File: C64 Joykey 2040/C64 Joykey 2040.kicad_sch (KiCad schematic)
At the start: 21 parts, among them J4 Expansion, M1 Mounting, M2 Mounting, M3 Mounting, M4 Mounting, U1 RP2040-Zero

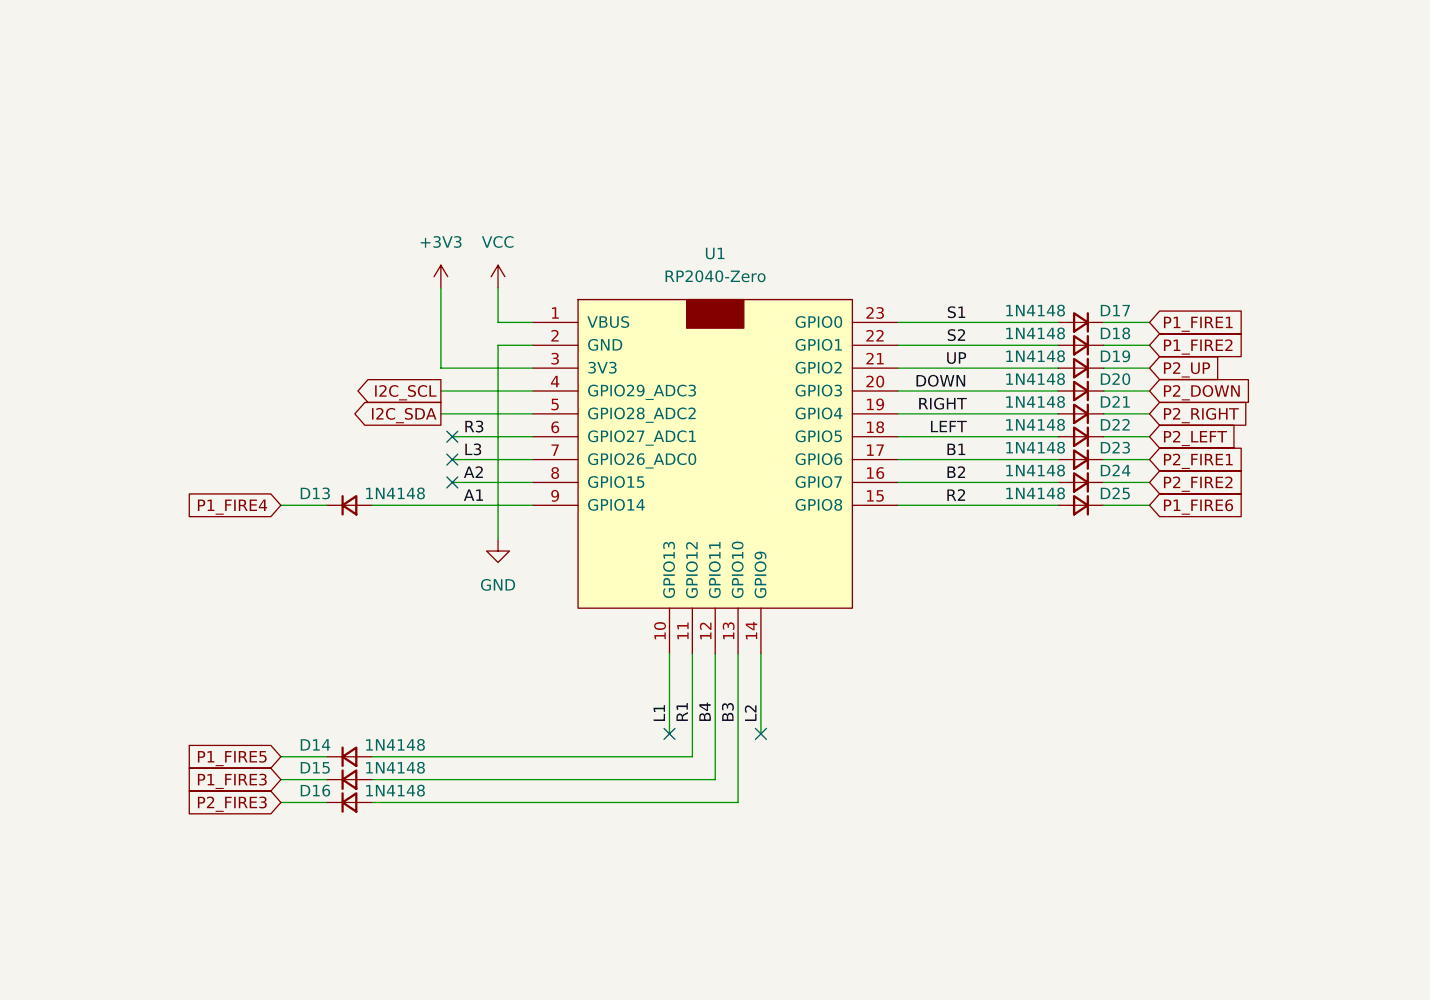
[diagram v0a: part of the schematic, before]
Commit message: Add diode for power from USB
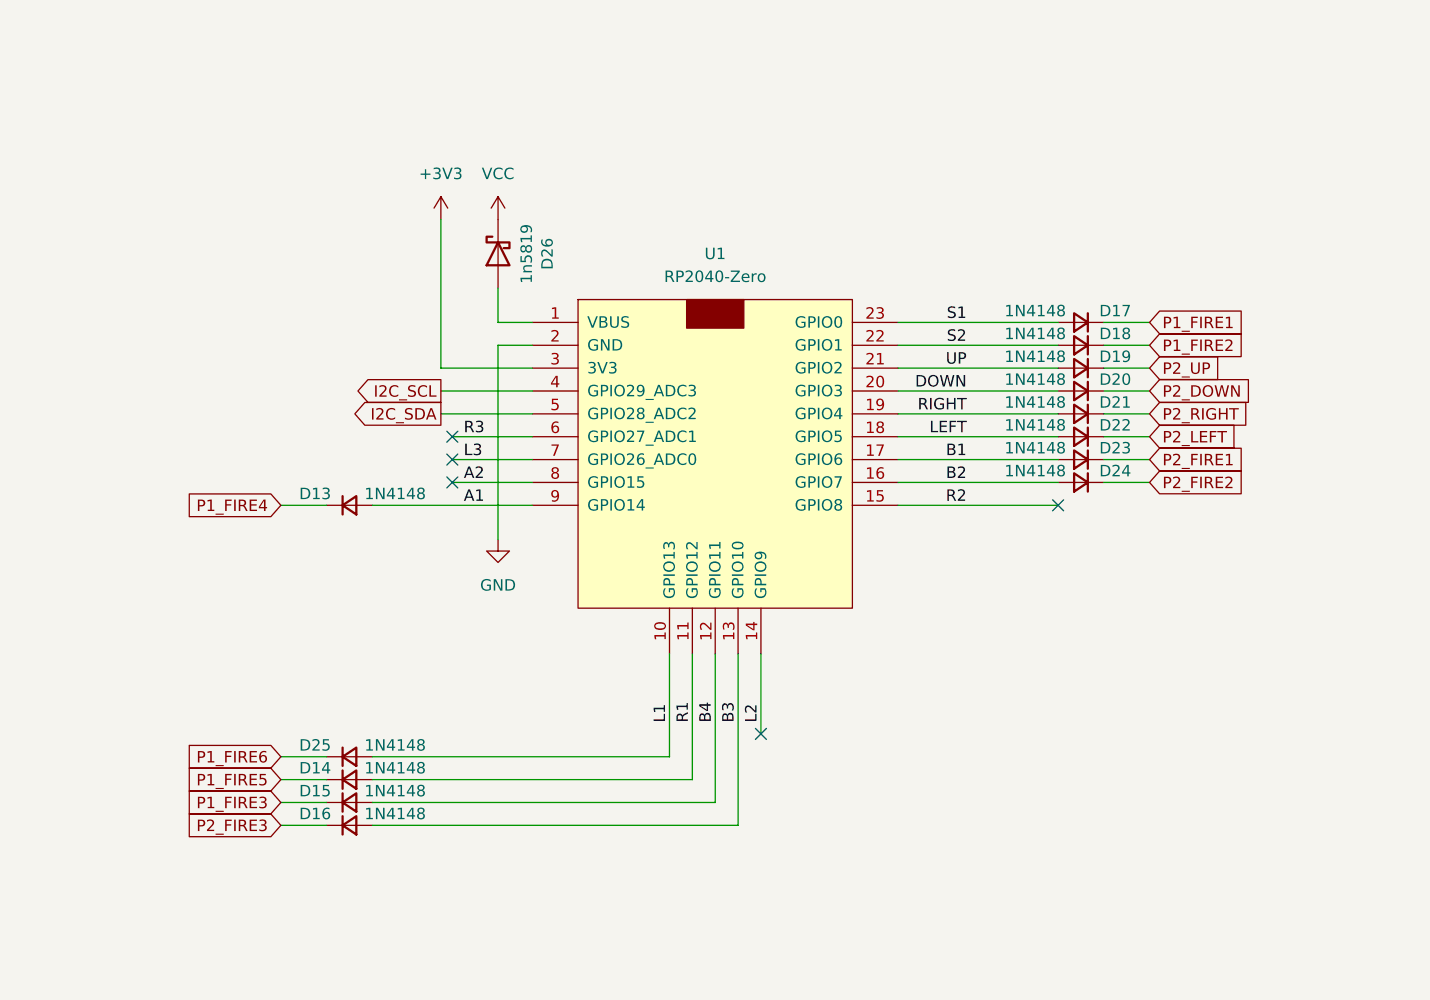
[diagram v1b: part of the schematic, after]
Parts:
- added D26: 1n5819, Diode_THT:D_DO-41_SOD81_P10.16mm_Horizontal, symbol Diode:1N5819
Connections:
- net L1: now also D25.2 (A)
- net R2: no longer D25.2 (A)
- net VCC: now also D26.1 (K); no longer U1.1 (VBUS)
- new net: D26.2 (A), U1.1 (VBUS)
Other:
- moved on the sheet: D14, D15, D16, D25

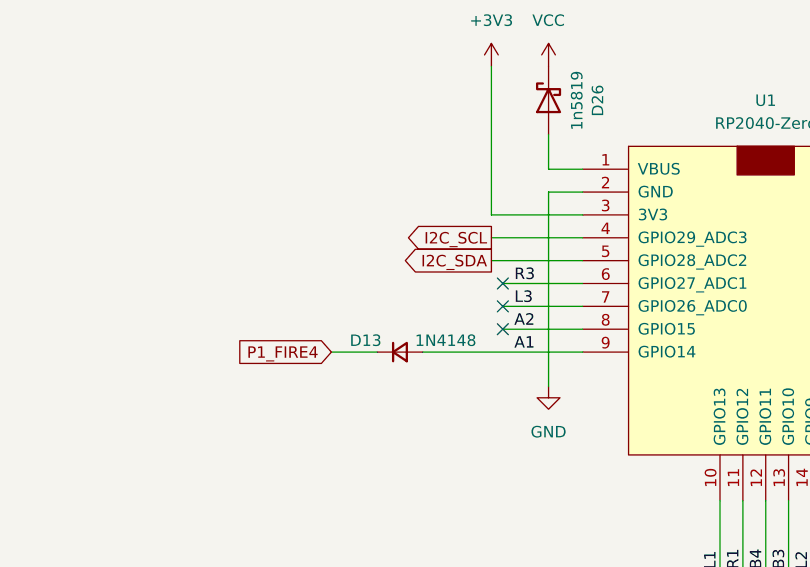
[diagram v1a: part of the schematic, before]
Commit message: Try adding underglow to GPIO15
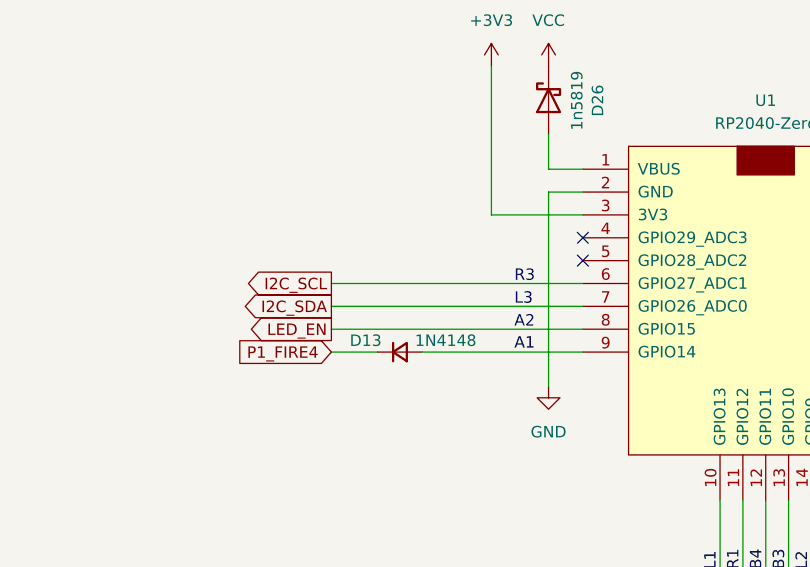
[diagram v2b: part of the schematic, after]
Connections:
- net L3 is gone; now on net I2C_SDA: U1.7 (GPIO26_ADC0)
- net R3 is gone; now on net I2C_SCL: U1.6 (GPIO27_ADC1)
- net I2C_SCL: no longer U1.4 (GPIO29_ADC3)
- net I2C_SDA: no longer U1.5 (GPIO28_ADC2)
- net A2 renamed LED_EN
- no-connect marks 5 -> 4
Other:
- note added: "A2"
- note added: "L3"
- note added: "R3"
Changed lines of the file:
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@@
-	)
-	(no_connect
-		(at 195.58 139.7)
 	)
 	(no_connect
@@
 	)
 	(no_connect
-		(at 195.58 137.16)
+		(at 204.47 132.08)
 	)
 	(no_connect
-		(at 195.58 142.24)
+		(at 204.47 134.62)
 	)
 	(wire
@@
 	(wire
 		(pts
-			(xy 195.58 139.7) (xy 204.47 139.7)
-		)
-		(stroke
-			(width 0)
-			(type default)
-		)
-	)
-	(wire
-		(pts
 			(xy 372.11 19.05) (xy 372.11 21.59)
 		)
@@
 	(wire
 		(pts
+			(xy 176.53 142.24) (xy 204.47 142.24)
+		)
+		(stroke
+			(width 0)
+			(type default)
+		)
+	)
+	(wire
+		(pts
 			(xy 381 21.59) (xy 381 19.05)
 		)
@@
 	(wire
 		(pts
+			(xy 176.53 139.7) (xy 204.47 139.7)
+		)
+		(stroke
+			(width 0)
+			(type default)
+		)
+	)
+	(wire
+		(pts
 			(xy 204.47 124.46) (xy 200.66 124.46)
 		)
@@
 	(wire
 		(pts
-			(xy 195.58 137.16) (xy 204.47 137.16)
-		)
-		(stroke
-			(width 0)
-			(type default)
-		)
-	)
-	(wire
-		(pts
 			(xy 393.7 24.13) (xy 397.51 24.13)
 		)
@@
 	(wire
 		(pts
-			(xy 194.31 132.08) (xy 204.47 132.08)
-		)
-		(stroke
-			(width 0)
-			(type default)
-		)
-	)
-	(wire
-		(pts
 			(xy 337.82 143.51) (xy 341.63 143.51)
 		)
@@
 	(wire
 		(pts
-			(xy 194.31 134.62) (xy 204.47 134.62)
-		)
-		(stroke
-			(width 0)
-			(type default)
-		)
-	)
-	(wire
-		(pts
 			(xy 181.61 177.8) (xy 176.53 177.8)
 		)
@@
 	(wire
 		(pts
-			(xy 195.58 142.24) (xy 204.47 142.24)
-		)
-		(stroke
-			(width 0)
-			(type default)
-		)
-	)
-	(wire
-		(pts
 			(xy 397.51 24.13) (xy 401.32 24.13)
 		)
@@
 	(wire
 		(pts
+			(xy 176.53 137.16) (xy 204.47 137.16)
+		)
+		(stroke
+			(width 0)
+			(type default)
+		)
+	)
+	(wire
+		(pts
 			(xy 245.11 127) (xy 262.89 127)
 		)
@@
 			(width 0)
 			(type default)
+		)
+	)
+	(text "A2"
+		(exclude_from_sim no)
+		(at 196.85 142.24 0)
+		(effects
+			(font
+				(size 1.27 1.27)
+			)
+			(justify left bottom)
+		)
+	)
+	(text "L3"
+		(exclude_from_sim no)
+		(at 196.85 139.7 0)
+		(effects
+			(font
+				(size 1.27 1.27)
+			)
+			(justify left bottom)
+		)
+	)
+	(text "R3"
+		(exclude_from_sim no)
+		(at 196.85 137.16 0)
+		(effects
+			(font
+				(size 1.27 1.27)
+			)
+			(justify left bottom)
 		)
 	)
@@
 		)
 	)
-	(label "A2"
-		(at 196.85 142.24 0)
-		(fields_autoplaced yes)
-		(effects
-			(font
-				(size 1.27 1.27)
-			)
-			(justify left bottom)
-		)
-	)
 	(label "B3"
 		(at 227.33 168.91 90)
@@
 		)
 	)
-	(label "R3"
-		(at 196.85 137.16 0)
-		(fields_autoplaced yes)
-		(effects
-			(font
-				(size 1.27 1.27)
-			)
-			(justify left bottom)
-		)
-	)
 	(label "L1"
 		(at 219.71 168.91 90)
@@
 		)
 	)
-	(label "L3"
-		(at 196.85 139.7 0)
-		(fields_autoplaced yes)
-		(effects
-			(font
-				(size 1.27 1.27)
-			)
-			(justify left bottom)
-		)
-	)
 	(label "RIGHT"
 		(at 252.73 134.62 180)
@@
 	(global_label "I2C_SCL"
 		(shape output)
-		(at 194.31 132.08 180)
+		(at 176.53 137.16 180)
 		(fields_autoplaced yes)
 		(effects
@@
 		)
 		(property "Intersheetrefs" "${INTERSHEET_REFS}"
-			(at 184.4195 132.08 0)
+			(at 166.6395 137.16 0)
 			(effects
 				(font
@@
 	(global_label "I2C_SDA"
 		(shape output)
-		(at 194.31 134.62 180)
+		(at 176.53 139.7 180)
 		(fields_autoplaced yes)
 		(effects
@@
 		)
 		(property "Intersheetrefs" "${INTERSHEET_REFS}"
-			(at 184.359 134.62 0)
+			(at 166.579 139.7 0)
 			(effects
 				(font
@@
 			(effects
 				(font
+					(size 1.27 1.27)
+				)
+				(hide yes)
+			)
+		)
+	)
+	(global_label "LED_EN"
+		(shape output)
+		(at 176.53 142.24 180)
+		(effects
+			(font
+				(size 1.27 1.27)
+			)
+			(justify right)
+		)
+		(property "Intersheetrefs" "${INTERSHEET_REFS}"
+			(at 176.53 142.24 0)
+			(effects
+				(font

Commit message: Slight build tweaks for clarity
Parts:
- U1: footprint pi_pico:RP2040-Zero -> pi_pico:RP2040-Zero-THT
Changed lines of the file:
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@@
 			)
 		)
-		(property "Footprint" "pi_pico:RP2040-Zero"
+		(property "Footprint" "pi_pico:RP2040-Zero-THT"
 			(at 224.79 120.65 0)
 			(effects
